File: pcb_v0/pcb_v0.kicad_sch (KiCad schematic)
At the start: 1 part, among them U1 ATtiny2313-20P

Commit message: Added symbols for 74141 and in-8
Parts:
- added NIX1, NIX2, NIX3, NIX4, NIX5, NIX6: ~, symbol nixie_symbols:in-8
- added U2, U3, U4, U5, U6, U7: 74141, Package_DIP:DIP-16_W7.62mm_LongPads, symbol nixie_symbols:74141
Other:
- moved on the sheet: U1

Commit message: saved
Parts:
- removed U5: 74141, Package_DIP:DIP-16_W7.62mm_LongPads, symbol nixie_symbols:74141
- added J1: Screw_Terminal_01x03, TerminalBlock_MetzConnect:TerminalBlock_MetzConnect_Type055_RT01503HDWU_1x03_P5.00mm_Horizontal, symbol Connector:Screw_Terminal_01x03
- added R1, R2, R3, R4, R5, R6: R_US, symbol Device:R_US
- added U10: 74141, Package_DIP:DIP-16_W7.62mm_LongPads, symbol nixie_symbols:74141
- added U5, U8, U9: 74LS377, Package_DIP:DIP-20_W7.62mm_LongPads, symbol 74xx:74LS377
- NIX1, NIX2, NIX3, NIX4, NIX5, NIX6: footprint (none) -> nixie:in-8
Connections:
- net at NIX3.0 (cathode0): now also U4.16 (~{Q0})
- net at NIX3.1 (cathode1): now also U4.15 (~{Q1})
- net at NIX3.10 (anode): now also R3.1
- net at NIX3.2 (cathode2): now also U4.8 (~{Q2})
- net at NIX3.3 (cathode3): now also U4.9 (~{Q3})
- net at NIX3.4 (cathode4): now also U4.13 (~{Q4})
- net at NIX3.5 (cathode5): now also U4.14 (~{Q5})
- net at NIX3.6 (cathode6): now also U4.11 (~{Q6})
- net at NIX3.7 (cathode7): now also U4.10 (~{Q7})
- net at NIX3.8 (cathode8): now also U4.1 (~{Q8})
- net at NIX3.9 (cathode9): now also U4.2 (~{Q9})
- net at U7.1 (~{Q8}): now also NIX5.8 (cathode8)
- net at U7.10 (~{Q7}): now also NIX5.7 (cathode7)
- net at U7.11 (~{Q6}): now also NIX5.6 (cathode6)
- net GND: now reaches U7.12 (GND)
- net GND: now also U1.10 (GND), U2.12 (GND), U3.12 (GND), U4.12 (GND), U6.12 (GND), J1.1 (Pin_1), U10.12 (GND), U5.1 (~{E}), U5.10 (GND), U8.1 (~{E}), U8.10 (GND), U9.1 (~{E}), U9.10 (GND)
- net at U7.13 (~{Q4}): now also NIX5.4 (cathode4)
- net at U7.14 (~{Q5}): now also NIX5.5 (cathode5)
- net at U7.15 (~{Q1}): now also NIX5.1 (cathode1)
- net at U7.16 (~{Q0}): now also NIX5.0 (cathode0)
- net at U7.2 (~{Q9}): now also NIX5.9 (cathode9)
- net at U7.3 (A): now also U9.2 (Q0)
- net at U7.4 (D): now also U9.9 (Q3)
- net +5V: now reaches U7.5 (VCC)
- net +5V: now also U1.20 (VCC), U2.5 (VCC), U3.5 (VCC), U4.5 (VCC), U6.5 (VCC), J1.2 (Pin_2), U10.5 (VCC), U5.20 (VCC), U8.20 (VCC), U9.20 (VCC)
- net at U7.6 (B): now also U9.5 (Q1)
- net at U7.7 (C): now also U9.6 (Q2)
- net at U7.8 (~{Q2}): now also NIX5.2 (cathode2)
- net at U7.9 (~{Q3}): now also NIX5.3 (cathode3)
- net at U2.1 (~{Q8}): now also NIX1.8 (cathode8)
- net at U2.10 (~{Q7}): now also NIX1.7 (cathode7)
- net at U2.11 (~{Q6}): now also NIX1.6 (cathode6)
- net at U2.13 (~{Q4}): now also NIX1.4 (cathode4)
- net at U2.14 (~{Q5}): now also NIX1.5 (cathode5)
- net at U2.15 (~{Q1}): now also NIX1.1 (cathode1)
- net at U2.16 (~{Q0}): now also NIX1.0 (cathode0)
- net at U2.2 (~{Q9}): now also NIX1.9 (cathode9)
- net at U2.3 (A): now also U8.2 (Q0)
- net at U2.4 (D): now also U8.9 (Q3)
- net at U2.6 (B): now also U8.5 (Q1)
- net at U2.7 (C): now also U8.6 (Q2)
- net at U2.8 (~{Q2}): now also NIX1.2 (cathode2)
- net at U2.9 (~{Q3}): now also NIX1.3 (cathode3)
- net at NIX4.0 (cathode0): now also U6.16 (~{Q0})
- net at NIX4.1 (cathode1): now also U6.15 (~{Q1})
- net at NIX4.10 (anode): now also R4.1
- net at NIX4.2 (cathode2): now also U6.8 (~{Q2})
- net at NIX4.3 (cathode3): now also U6.9 (~{Q3})
- net at NIX4.4 (cathode4): now also U6.13 (~{Q4})
- net at NIX4.5 (cathode5): now also U6.14 (~{Q5})
- net at NIX4.6 (cathode6): now also U6.11 (~{Q6})
- net at NIX4.7 (cathode7): now also U6.10 (~{Q7})
- net at NIX4.8 (cathode8): now also U6.1 (~{Q8})
- net at NIX4.9 (cathode9): now also U6.2 (~{Q9})
- net at NIX1.10 (anode): now also R1.1
- net at U6.3 (A): now also U5.12 (Q4)
- net at U6.4 (D): now also U5.19 (Q7)
- net at U6.6 (B): now also U5.15 (Q5)
- net at U6.7 (C): now also U5.16 (Q6)
- net at NIX6.0 (cathode0): now also U10.16 (~{Q0})
- net at NIX6.1 (cathode1): now also U10.15 (~{Q1})
- net at NIX6.10 (anode): now also R6.1
- net at NIX6.2 (cathode2): now also U10.8 (~{Q2})
- net at NIX6.3 (cathode3): now also U10.9 (~{Q3})
- net at NIX6.4 (cathode4): now also U10.13 (~{Q4})
- net at NIX6.5 (cathode5): now also U10.14 (~{Q5})
- net at NIX6.6 (cathode6): now also U10.11 (~{Q6})
- net at NIX6.7 (cathode7): now also U10.10 (~{Q7})
- net at NIX6.8 (cathode8): now also U10.1 (~{Q8})
- net at NIX6.9 (cathode9): now also U10.2 (~{Q9})
- net at NIX5.10 (anode): now also R5.1
- net at U3.1 (~{Q8}): now also NIX2.8 (cathode8)
- net at U3.10 (~{Q7}): now also NIX2.7 (cathode7)
- net at U3.11 (~{Q6}): now also NIX2.6 (cathode6)
- net at U3.13 (~{Q4}): now also NIX2.4 (cathode4)
- net at U3.14 (~{Q5}): now also NIX2.5 (cathode5)
- net at U3.15 (~{Q1}): now also NIX2.1 (cathode1)
- net at U3.16 (~{Q0}): now also NIX2.0 (cathode0)
- net at U3.2 (~{Q9}): now also NIX2.9 (cathode9)
- net at U3.3 (A): now also U8.12 (Q4)
- net at U3.4 (D): now also U8.19 (Q7)
- net at U3.6 (B): now also U8.15 (Q5)
- net at U3.7 (C): now also U8.16 (Q6)
- net at U3.8 (~{Q2}): now also NIX2.2 (cathode2)
- net at U3.9 (~{Q3}): now also NIX2.3 (cathode3)
- net at U4.3 (A): now also U5.2 (Q0)
- net at U4.4 (D): now also U5.9 (Q3)
- net at U4.6 (B): now also U5.5 (Q1)
- net at U4.7 (C): now also U5.6 (Q2)
- net at NIX2.10 (anode): now also R2.1
- net at U1.12 (PB0): now also U5.3 (D0), U8.3 (D0), U9.3 (D0)
- net at U1.13 (PB1): now also U5.4 (D1), U8.4 (D1), U9.4 (D1)
- net at U1.14 (PB2): now also U5.7 (D2), U8.7 (D2), U9.7 (D2)
- net at U1.15 (PB3): now also U5.8 (D3), U8.8 (D3), U9.8 (D3)
- net at U1.16 (PB4): now also U5.13 (D4), U8.13 (D4), U9.13 (D4)
- net at U1.17 (PB5): now also U5.14 (D5), U8.14 (D5), U9.14 (D5)
- net at U1.18 (PB6): now also U5.17 (D6), U8.17 (D6), U9.17 (D6)
- net at U1.19 (PB7): now also U5.18 (D7), U8.18 (D7), U9.18 (D7)
- new net: U10.3 (A), U9.12 (Q4)
- new net: U10.4 (D), U9.19 (Q7)
- new net: U10.6 (B), U9.15 (Q5)
- new net: U10.7 (C), U9.16 (Q6)
- new net hv: J1.3 (Pin_3), R1.2, R2.2, R3.2, R4.2, R5.2, R6.2
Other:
- moved on the sheet: NIX1, U1, U2

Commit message: saved
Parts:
- U1: footprint Package_DIP:DIP-20_W7.62mm -> Package_DIP:DIP-20_W7.62mm_LongPads
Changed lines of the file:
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@@
       (effects (font (size 1.27 1.27)) (justify left))
     )
-    (property "Footprint" "Package_DIP:DIP-20_W7.62mm" (at 250.19 121.92 0)
+    (property "Footprint" "Package_DIP:DIP-20_W7.62mm_LongPads" (at 250.19 121.92 0)
       (effects (font (size 1.27 1.27) italic) hide)
     )

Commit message: saved
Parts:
- U1, U5, U8, U9: footprint Package_DIP:DIP-20_W7.62mm_LongPads -> Package_DIP:DIP-20_W7.62mm
- U10, U2, U3, U4, U6, U7: footprint Package_DIP:DIP-16_W7.62mm_LongPads -> Package_DIP:DIP-16_W7.62mm
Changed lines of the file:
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@@
       (effects (font (size 1.27 1.27)))
     )
-    (property "Footprint" "Package_DIP:DIP-16_W7.62mm_LongPads" (at 412.115 277.495 0)
+    (property "Footprint" "Package_DIP:DIP-16_W7.62mm" (at 412.115 277.495 0)
       (effects (font (size 1.27 1.27)) hide)
     )
@@
       (effects (font (size 1.27 1.27)))
     )
-    (property "Footprint" "Package_DIP:DIP-16_W7.62mm_LongPads" (at 412.115 163.195 0)
+    (property "Footprint" "Package_DIP:DIP-16_W7.62mm" (at 412.115 163.195 0)
       (effects (font (size 1.27 1.27)) hide)
     )
@@
       (effects (font (size 1.27 1.27)) (justify left))
     )
-    (property "Footprint" "Package_DIP:DIP-20_W7.62mm_LongPads" (at 363.22 114.3 0)
+    (property "Footprint" "Package_DIP:DIP-20_W7.62mm" (at 363.22 114.3 0)
       (effects (font (size 1.27 1.27)) hide)
     )
@@
       (effects (font (size 1.27 1.27)))
     )
-    (property "Footprint" "Package_DIP:DIP-16_W7.62mm_LongPads" (at 412.115 125.095 0)
+    (property "Footprint" "Package_DIP:DIP-16_W7.62mm" (at 412.115 125.095 0)
       (effects (font (size 1.27 1.27)) hide)
     )
@@
       (effects (font (size 1.27 1.27)) (justify left))
     )
-    (property "Footprint" "Package_DIP:DIP-20_W7.62mm_LongPads" (at 363.22 190.5 0)
+    (property "Footprint" "Package_DIP:DIP-20_W7.62mm" (at 363.22 190.5 0)
       (effects (font (size 1.27 1.27)) hide)
     )
@@
       (effects (font (size 1.27 1.27)))
     )
-    (property "Footprint" "Package_DIP:DIP-16_W7.62mm_LongPads" (at 412.115 315.595 0)
+    (property "Footprint" "Package_DIP:DIP-16_W7.62mm" (at 412.115 315.595 0)
       (effects (font (size 1.27 1.27)) hide)
     )
@@
       (effects (font (size 1.27 1.27)))
     )
-    (property "Footprint" "Package_DIP:DIP-16_W7.62mm_LongPads" (at 412.115 239.395 0)
+    (property "Footprint" "Package_DIP:DIP-16_W7.62mm" (at 412.115 239.395 0)
       (effects (font (size 1.27 1.27)) hide)
     )
@@
       (effects (font (size 1.27 1.27)))
     )
-    (property "Footprint" "Package_DIP:DIP-16_W7.62mm_LongPads" (at 412.115 201.295 0)
+    (property "Footprint" "Package_DIP:DIP-16_W7.62mm" (at 412.115 201.295 0)
       (effects (font (size 1.27 1.27)) hide)
     )
@@
       (effects (font (size 1.27 1.27)) (justify left))
     )
-    (property "Footprint" "Package_DIP:DIP-20_W7.62mm_LongPads" (at 363.22 266.7 0)
+    (property "Footprint" "Package_DIP:DIP-20_W7.62mm" (at 363.22 266.7 0)
       (effects (font (size 1.27 1.27)) hide)
     )
@@
       (effects (font (size 1.27 1.27)) (justify left))
     )
-    (property "Footprint" "Package_DIP:DIP-20_W7.62mm_LongPads" (at 250.19 121.92 0)
+    (property "Footprint" "Package_DIP:DIP-20_W7.62mm" (at 250.19 121.92 0)
       (effects (font (size 1.27 1.27) italic) hide)
     )

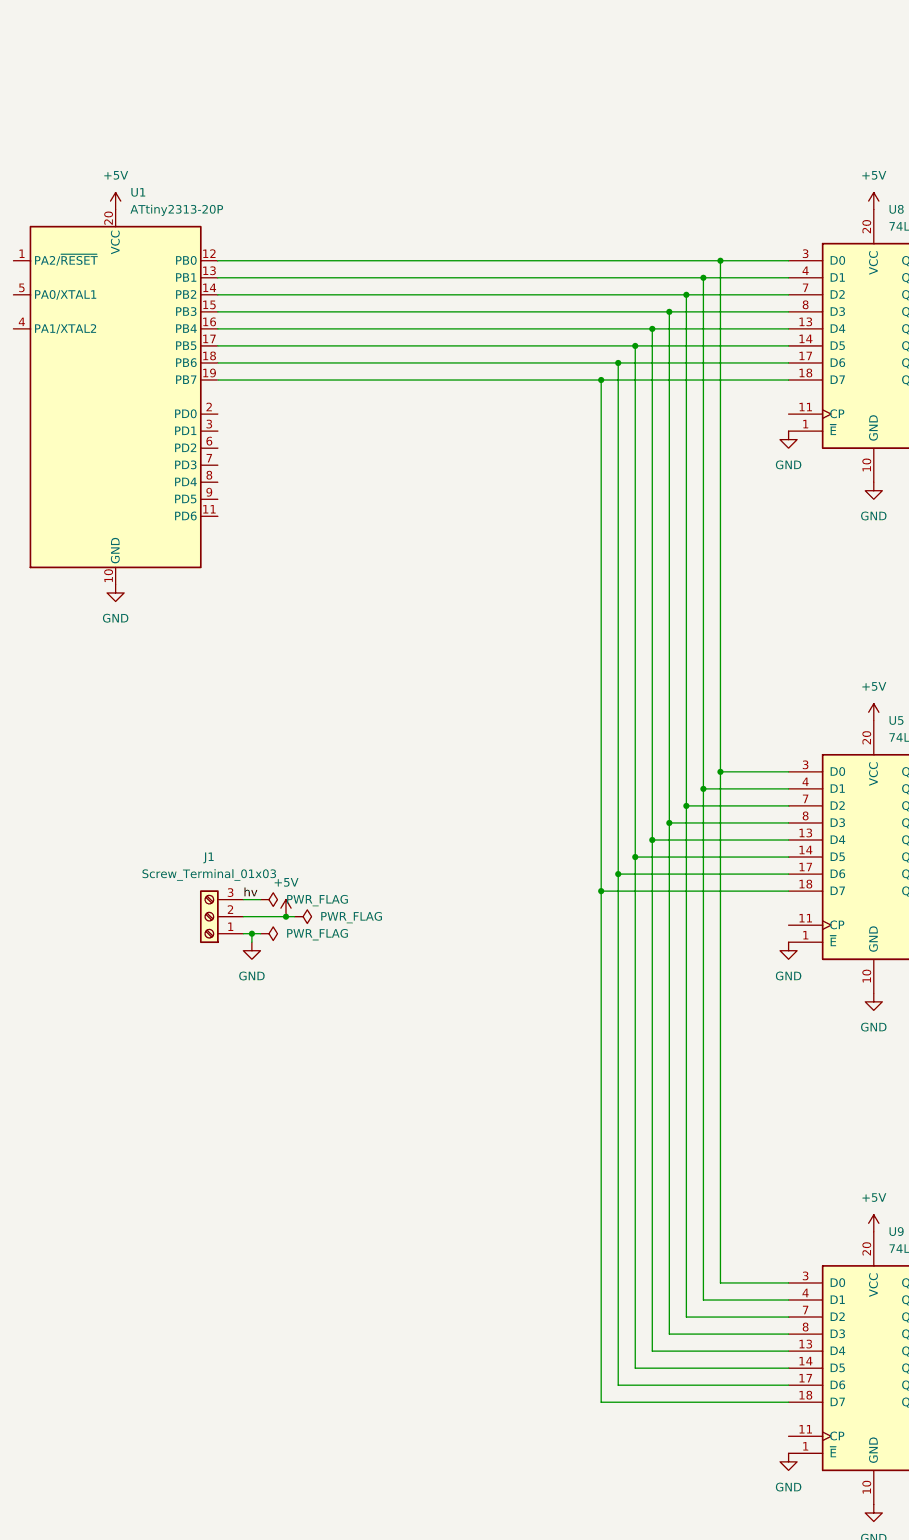
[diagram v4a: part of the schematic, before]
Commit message: ATtiny and flip flops routed
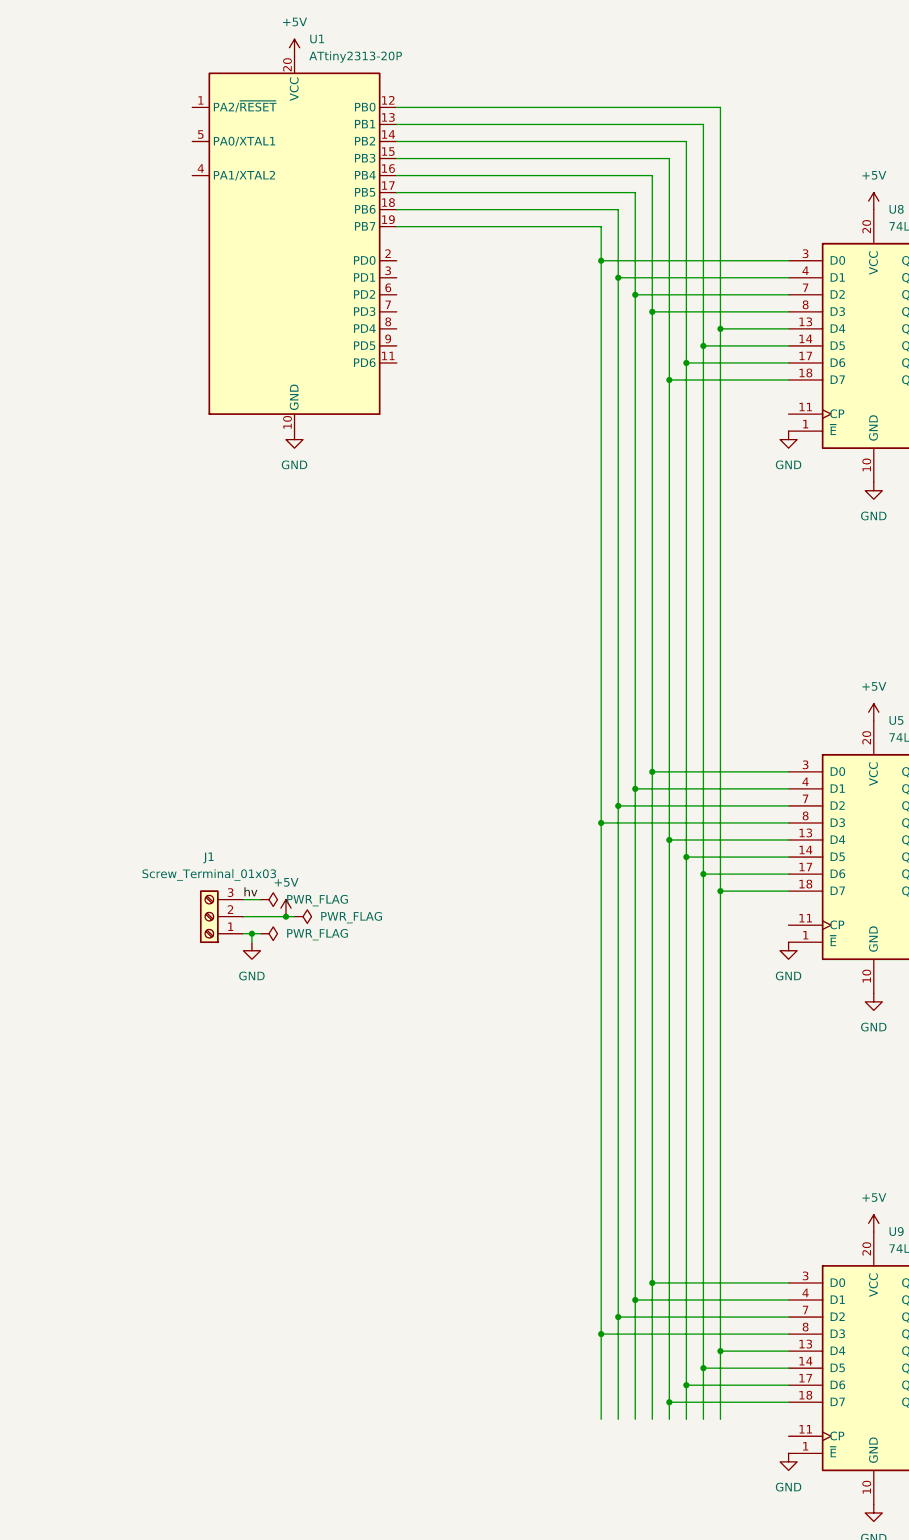
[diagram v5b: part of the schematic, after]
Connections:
- net at U8.13 (D4), U9.13 (D4): now also U1.12 (PB0), U5.18 (D7); no longer U1.16 (PB4), U5.13 (D4)
- net at U8.14 (D5), U9.14 (D5): now also U1.13 (PB1), U5.17 (D6); no longer U1.17 (PB5), U5.14 (D5)
- net at U8.17 (D6), U9.17 (D6): now also U1.14 (PB2), U5.14 (D5); no longer U1.18 (PB6), U5.17 (D6)
- net at U8.18 (D7), U9.18 (D7): now also U1.15 (PB3), U5.13 (D4); no longer U1.19 (PB7), U5.18 (D7)
- net at U5.3 (D0), U9.3 (D0): now also U1.16 (PB4), U8.8 (D3); no longer U1.12 (PB0), U8.3 (D0)
- net at U5.4 (D1), U9.4 (D1): now also U1.17 (PB5), U8.7 (D2); no longer U1.13 (PB1), U8.4 (D1)
- net at U5.7 (D2), U9.7 (D2): now also U1.18 (PB6), U8.4 (D1); no longer U1.14 (PB2), U8.7 (D2)
- net at U5.8 (D3), U9.8 (D3): now also U1.19 (PB7), U8.3 (D0); no longer U1.15 (PB3), U8.8 (D3)
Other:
- moved on the sheet: U1

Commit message: save
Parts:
- added NE1, NE2: Lamp_Neon, Connector_PinSocket_1.27mm:PinSocket_1x02_P1.27mm_Vertical, symbol Device:Lamp_Neon
- added Q1: Q_NMOS_GDS, Package_TO_SOT_SMD:SOT-223-3_TabPin2, symbol Device:Q_NMOS_GDS
- added R7, R8: R_US, Resistor_THT:R_Axial_DIN0204_L3.6mm_D1.6mm_P2.54mm_Vertical, symbol Device:R_US
- J1: footprint TerminalBlock_MetzConnect:TerminalBlock_MetzConnect_Type055_RT01503HDWU_1x03_P5.00mm_Horizontal -> Connector_PinHeader_2.54mm:PinHeader_1x03_P2.54mm_Vertical
- R1, R2, R3, R4, R5, R6: footprint (none) -> Resistor_THT:R_Axial_DIN0204_L3.6mm_D1.6mm_P2.54mm_Vertical
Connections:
- net GND: now also Q1.3 (S)
- net hv: now also NE1.2, NE2.2
- net at U1.12 (PB0), U5.18 (D7), U9.13 (D4): now also U8.8 (D3); no longer U8.13 (D4)
- net at U1.13 (PB1), U5.17 (D6), U9.14 (D5): now also U8.7 (D2); no longer U8.14 (D5)
- net at U1.14 (PB2), U5.14 (D5), U9.17 (D6): now also U8.4 (D1); no longer U8.17 (D6)
- net at U1.15 (PB3), U5.13 (D4), U9.18 (D7): now also U8.3 (D0); no longer U8.18 (D7)
- net at U1.19 (PB7), U5.8 (D3), U9.8 (D3): now also U8.13 (D4); no longer U8.3 (D0)
- net at U1.18 (PB6), U5.7 (D2), U9.7 (D2): now also U8.14 (D5); no longer U8.4 (D1)
- net at U1.17 (PB5), U5.4 (D1), U9.4 (D1): now also U8.17 (D6); no longer U8.7 (D2)
- net at U1.16 (PB4), U5.3 (D0), U9.3 (D0): now also U8.18 (D7); no longer U8.8 (D3)
- new net: NE1.1, R7.2
- new net: Q1.2 (D), R7.1, R8.1
- new net: NE2.1, R8.2

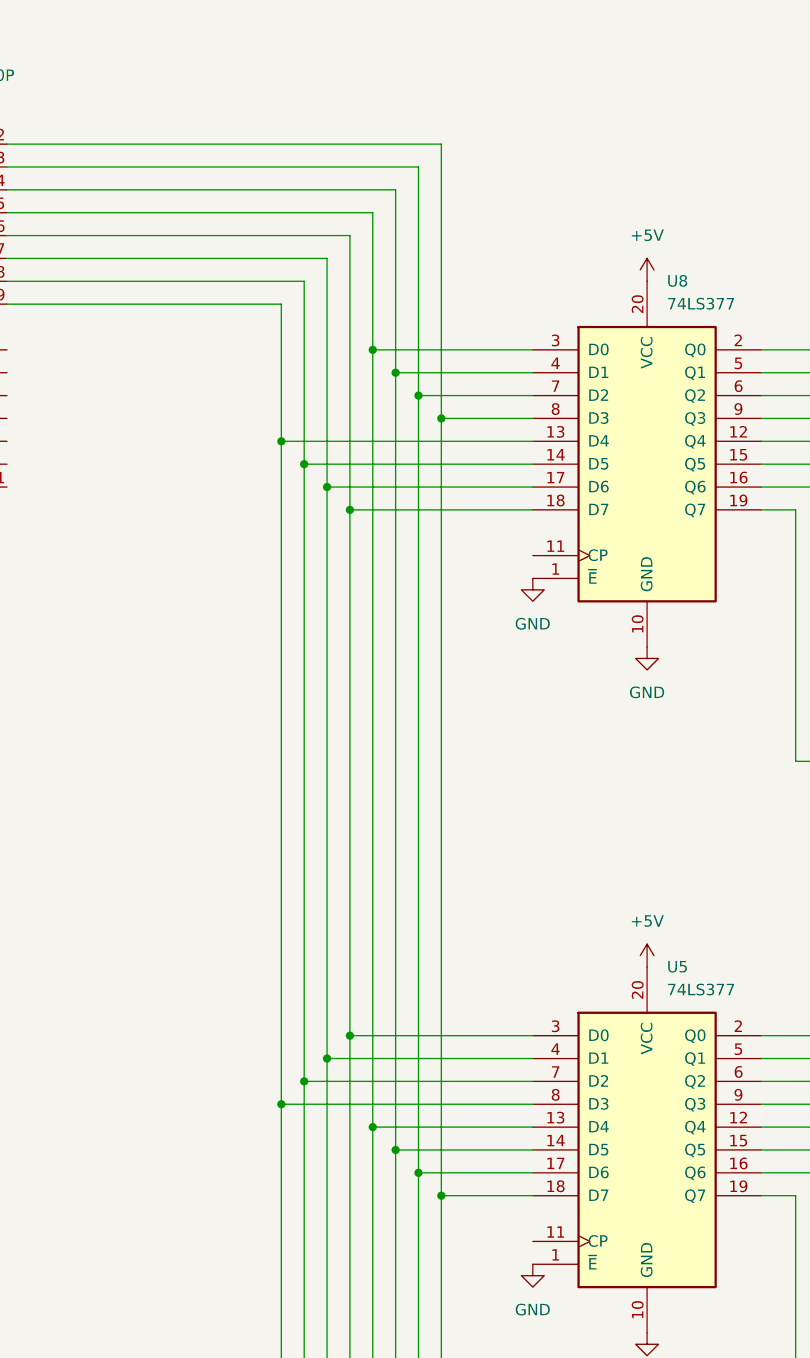
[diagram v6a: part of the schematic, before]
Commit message: registers wired correctly this time
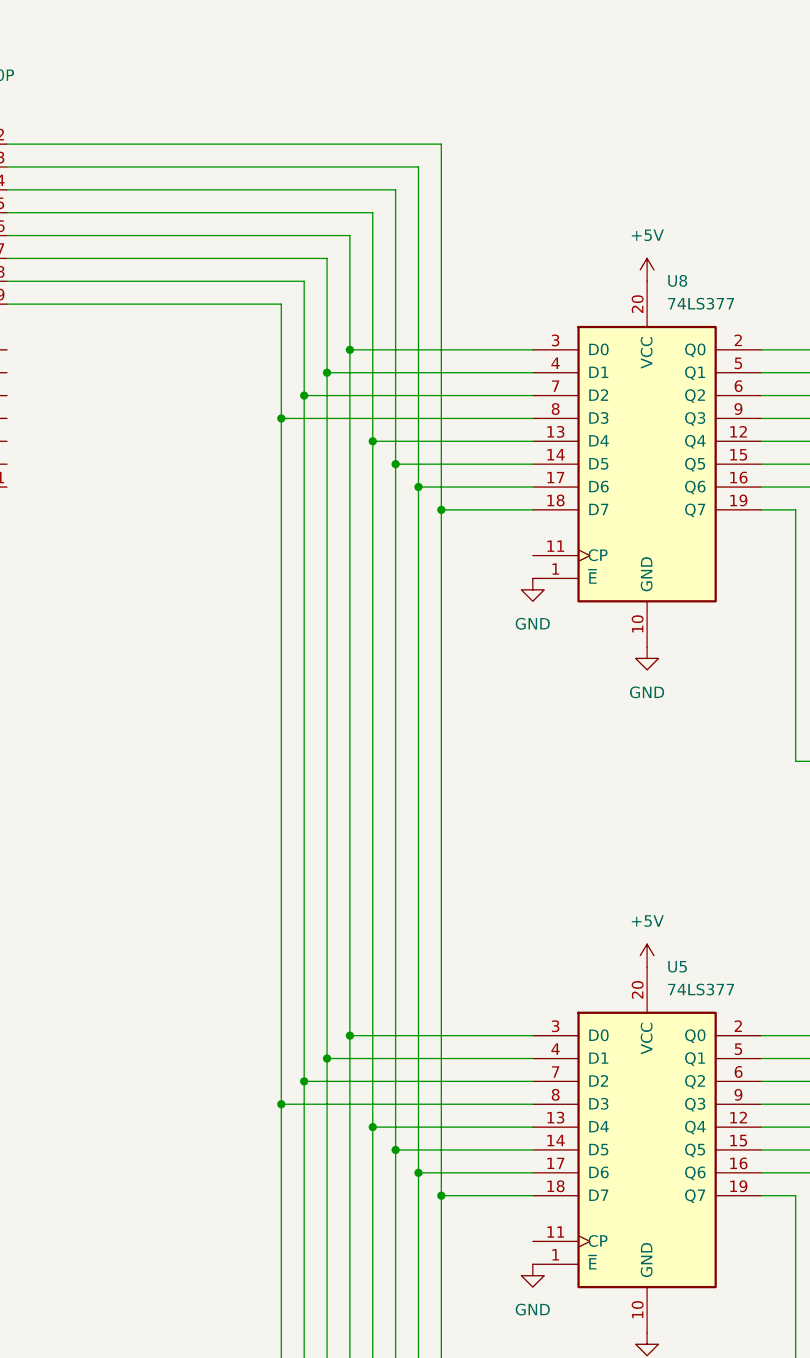
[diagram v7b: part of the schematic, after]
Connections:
- net at U1.19 (PB7), U5.8 (D3), U9.8 (D3): now also U8.8 (D3); no longer U8.13 (D4)
- net at U1.18 (PB6), U5.7 (D2), U9.7 (D2): now also U8.7 (D2); no longer U8.14 (D5)
- net at U1.17 (PB5), U5.4 (D1), U9.4 (D1): now also U8.4 (D1); no longer U8.17 (D6)
- net at U1.16 (PB4), U5.3 (D0), U9.3 (D0): now also U8.3 (D0); no longer U8.18 (D7)
- net at U1.15 (PB3), U5.13 (D4), U9.18 (D7): now also U8.13 (D4); no longer U8.3 (D0)
- net at U1.14 (PB2), U5.14 (D5), U9.17 (D6): now also U8.14 (D5); no longer U8.4 (D1)
- net at U1.13 (PB1), U5.17 (D6), U9.14 (D5): now also U8.17 (D6); no longer U8.7 (D2)
- net at U1.12 (PB0), U5.18 (D7), U9.13 (D4): now also U8.18 (D7); no longer U8.8 (D3)
